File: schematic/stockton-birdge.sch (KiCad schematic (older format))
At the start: 18 parts, among them J5 Conn_Coaxial, J6 Conn_Coaxial, J7 Conn_Coaxial, J8 Conn_Coaxial

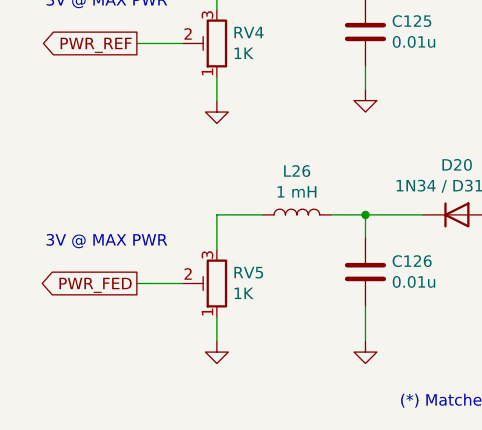
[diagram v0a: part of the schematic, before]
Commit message: Fix typo: PWR_FED -> PWR_FWD
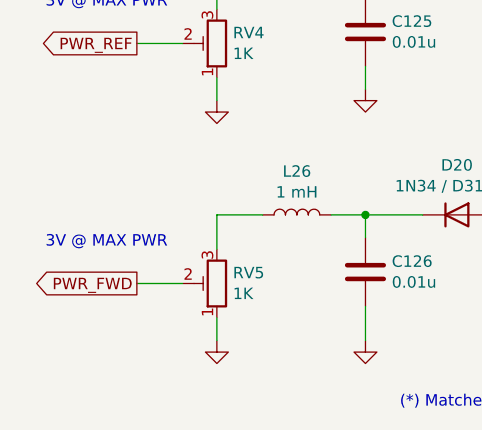
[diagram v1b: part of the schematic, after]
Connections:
- net PWR_FED renamed PWR_FWD
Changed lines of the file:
@@
 	3150 3300 3350 3300
 Text GLabel 2800 4700 0    50   Output ~ 0
-PWR_FED
+PWR_FWD
 Text GLabel 2800 3650 0    50   Output ~ 0
 PWR_REF

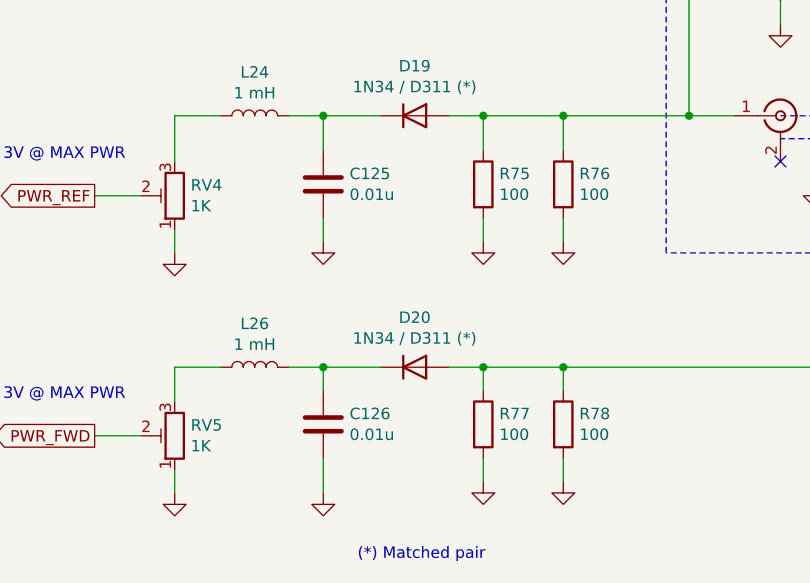
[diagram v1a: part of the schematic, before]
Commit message: Correct the schematic
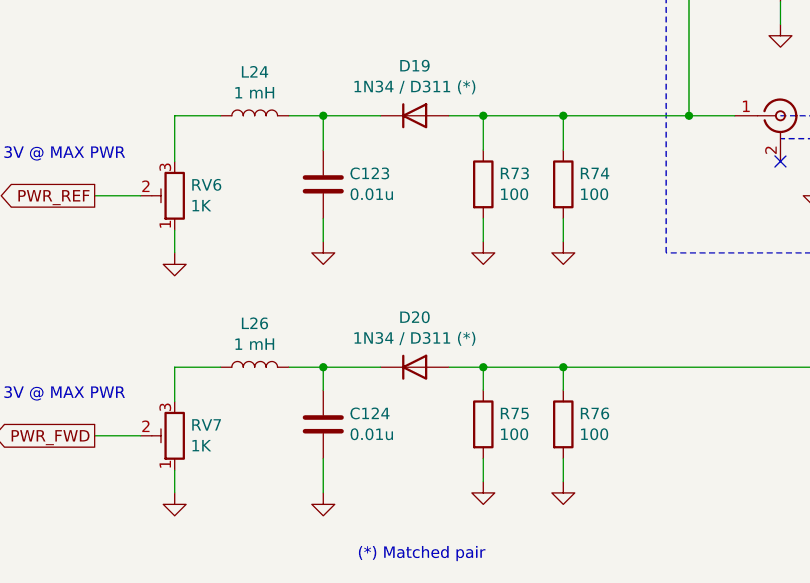
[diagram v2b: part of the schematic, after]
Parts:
- renumbered C125 to C123, C126 to C124, R75 to R73, R76 to R74, R77 to R75, R78 to R76, RV4 to RV6, RV5 to RV7
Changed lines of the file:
@@
 $EndComp
 $Comp
-L power:GND #PWR0170
+L power:GND #PWR0169
 U 1 1 6309B688
 P 5800 2900
-F 0 "#PWR0170" H 5800 2650 50  0001 C CNN
+F 0 "#PWR0169" H 5800 2650 50  0001 C CNN
 F 1 "GND" H 5805 2727 50  0001 C CNN
 F 2 "" H 5800 2900 50  0001 C CNN
@@
 $EndComp
 $Comp
-L power:GND #PWR0172
+L power:GND #PWR0171
 U 1 1 6309BAED
 P 6450 3650
-F 0 "#PWR0172" H 6450 3400 50  0001 C CNN
+F 0 "#PWR0171" H 6450 3400 50  0001 C CNN
 F 1 "GND" H 6455 3477 50  0001 C CNN
 F 2 "" H 6450 3650 50  0001 C CNN
@@
 $EndComp
 $Comp
-L power:GND #PWR0171
+L power:GND #PWR0170
 U 1 1 6309FD20
 P 5950 3600
-F 0 "#PWR0171" H 5950 3350 50  0001 C CNN
+F 0 "#PWR0170" H 5950 3350 50  0001 C CNN
 F 1 "GND" H 5955 3427 50  0001 C CNN
 F 2 "" H 5950 3600 50  0001 C CNN
@@
 	5950 3500 6000 3500
 $Comp
-L power:GND #PWR0169
+L power:GND #PWR0168
 U 1 1 630A0599
 P 6350 2400
-F 0 "#PWR0169" H 6350 2150 50  0001 C CNN
+F 0 "#PWR0168" H 6350 2150 50  0001 C CNN
 F 1 "GND" H 6355 2227 50  0001 C CNN
 F 2 "" H 6350 2400 50  0001 C CNN
@@
 STOCKTON_BRIDGE_OUT
 $Comp
-L Device:R R75
+L Device:R R73
 U 1 1 630A90B8
 P 4500 3600
-F 0 "R75" H 4570 3646 50  0000 L CNN
+F 0 "R73" H 4570 3646 50  0000 L CNN
 F 1 "100" H 4570 3555 50  0000 L CNN
 F 2 "" V 4430 3600 50  0001 C CNN
@@
 $EndComp
 $Comp
-L Device:R R76
+L Device:R R74
 U 1 1 630A99A2
 P 4850 3600
-F 0 "R76" H 4920 3646 50  0000 L CNN
+F 0 "R74" H 4920 3646 50  0000 L CNN
 F 1 "100" H 4920 3555 50  0000 L CNN
 F 2 "" V 4780 3600 50  0001 C CNN
@@
 $EndComp
 $Comp
-L power:GND #PWR0174
+L power:GND #PWR0173
 U 1 1 630A9CF0
 P 4500 3850
-F 0 "#PWR0174" H 4500 3600 50  0001 C CNN
+F 0 "#PWR0173" H 4500 3600 50  0001 C CNN
 F 1 "GND" H 4505 3677 50  0001 C CNN
 F 2 "" H 4500 3850 50  0001 C CNN
@@
 $EndComp
 $Comp
-L power:GND #PWR0175
+L power:GND #PWR0174
 U 1 1 630AA186
 P 4850 3850
-F 0 "#PWR0175" H 4850 3600 50  0001 C CNN
+F 0 "#PWR0174" H 4850 3600 50  0001 C CNN
 F 1 "GND" H 4855 3677 50  0001 C CNN
 F 2 "" H 4850 3850 50  0001 C CNN
@@
 $EndComp
 $Comp
-L Device:R R77
+L Device:R R75
 U 1 1 630AA604
 P 4500 4650
-F 0 "R77" H 4570 4696 50  0000 L CNN
+F 0 "R75" H 4570 4696 50  0000 L CNN
 F 1 "100" H 4570 4605 50  0000 L CNN
 F 2 "" V 4430 4650 50  0001 C CNN
@@
 $EndComp
 $Comp
-L Device:R R78
+L Device:R R76
 U 1 1 630AA60E
 P 4850 4650
-F 0 "R78" H 4920 4696 50  0000 L CNN
+F 0 "R76" H 4920 4696 50  0000 L CNN
 F 1 "100" H 4920 4605 50  0000 L CNN
 F 2 "" V 4780 4650 50  0001 C CNN
@@
 $EndComp
 $Comp
-L power:GND #PWR0177
+L power:GND #PWR0176
 U 1 1 630AA618
 P 4500 4900
-F 0 "#PWR0177" H 4500 4650 50  0001 C CNN
+F 0 "#PWR0176" H 4500 4650 50  0001 C CNN
 F 1 "GND" H 4505 4727 50  0001 C CNN
 F 2 "" H 4500 4900 50  0001 C CNN
@@
 $EndComp
 $Comp
-L power:GND #PWR0178
+L power:GND #PWR0177
 U 1 1 630AA622
 P 4850 4900
-F 0 "#PWR0178" H 4850 4650 50  0001 C CNN
+F 0 "#PWR0177" H 4850 4650 50  0001 C CNN
 F 1 "GND" H 4855 4727 50  0001 C CNN
 F 2 "" H 4850 4900 50  0001 C CNN
@@
 (*) Matched pair
 $Comp
-L Device:C C125
+L Device:C C123
 U 1 1 630B29EA
 P 3800 3600
-F 0 "C125" H 3915 3646 50  0000 L CNN
+F 0 "C123" H 3915 3646 50  0000 L CNN
 F 1 "0.01u" H 3915 3555 50  0000 L CNN
 F 2 "" H 3838 3450 50  0001 C CNN
@@
 $EndComp
 $Comp
-L Device:C C126
+L Device:C C124
 U 1 1 630B31F8
 P 3800 4650
-F 0 "C126" H 3915 4696 50  0000 L CNN
+F 0 "C124" H 3915 4696 50  0000 L CNN
 F 1 "0.01u" H 3915 4605 50  0000 L CNN
 F 2 "" H 3838 4500 50  0001 C CNN
@@
 $EndComp
 $Comp
-L power:GND #PWR0180
+L power:GND #PWR0179
 U 1 1 630B36AF
 P 3800 4950
-F 0 "#PWR0180" H 3800 4700 50  0001 C CNN
+F 0 "#PWR0179" H 3800 4700 50  0001 C CNN
 F 1 "GND" H 3805 4777 50  0001 C CNN
 F 2 "" H 3800 4950 50  0001 C CNN
@@
 	3800 4400 4050 4400
 $Comp
-L power:GND #PWR0173
+L power:GND #PWR0172
 U 1 1 630B4D9B
 P 3800 3850
-F 0 "#PWR0173" H 3800 3600 50  0001 C CNN
+F 0 "#PWR0172" H 3800 3600 50  0001 C CNN
 F 1 "GND" H 3805 3677 50  0001 C CNN
 F 2 "" H 3800 3850 50  0001 C CNN
@@
 Connection ~ 3800 3300
 $Comp
-L Device:R_POT_TRIM RV4
+L Device:R_POT_TRIM RV6
 U 1 1 630BC689
 P 3150 3650
-F 0 "RV4" H 3080 3604 50  0000 R CNN
+F 0 "RV6" H 3080 3604 50  0000 R CNN
 F 1 "1K" H 3080 3695 50  0000 R CNN
 F 2 "" H 3150 3650 50  0001 C CNN
@@
 $EndComp
 $Comp
-L Device:R_POT_TRIM RV5
+L Device:R_POT_TRIM RV7
 U 1 1 630BCE1A
 P 3150 4700
-F 0 "RV5" H 3080 4654 50  0000 R CNN
+F 0 "RV7" H 3080 4654 50  0000 R CNN
 F 1 "1K" H 3080 4745 50  0000 R CNN
 F 2 "" H 3150 4700 50  0001 C CNN
@@
 $EndComp
 $Comp
-L power:GND #PWR0176
+L power:GND #PWR0175
 U 1 1 630BE609
 P 3150 3900
-F 0 "#PWR0176" H 3150 3650 50  0001 C CNN
+F 0 "#PWR0175" H 3150 3650 50  0001 C CNN
 F 1 "GND" H 3155 3727 50  0001 C CNN
 F 2 "" H 3150 3900 50  0001 C CNN
@@
 $EndComp
 $Comp
-L power:GND #PWR0179
+L power:GND #PWR0178
 U 1 1 630BEAA6
 P 3150 4950
-F 0 "#PWR0179" H 3150 4700 50  0001 C CNN
+F 0 "#PWR0178" H 3150 4700 50  0001 C CNN
 F 1 "GND" H 3155 4777 50  0001 C CNN
 F 2 "" H 3150 4950 50  0001 C CNN
